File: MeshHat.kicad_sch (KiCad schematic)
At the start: 4 parts, among them J1 RPi_GPIO, U1 24LC256

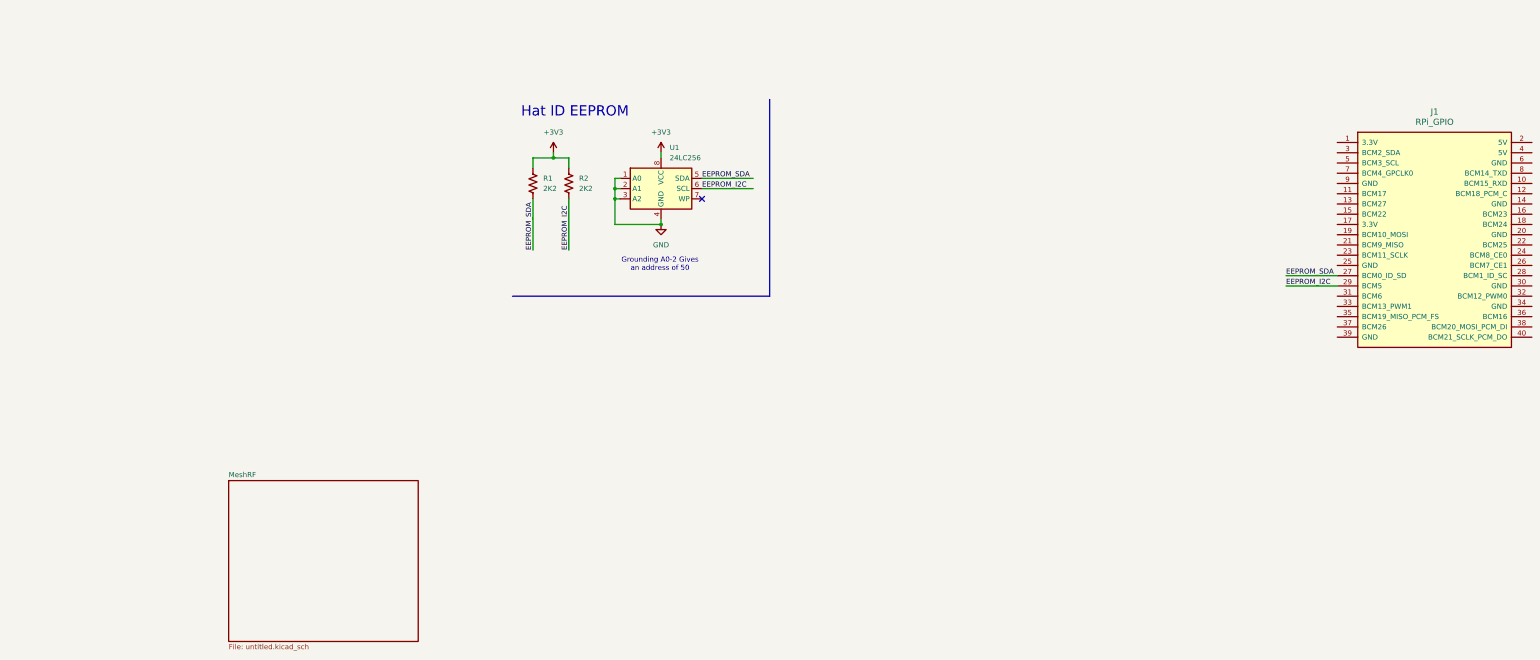
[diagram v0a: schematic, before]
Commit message: add the rest of the components and the OCD connections
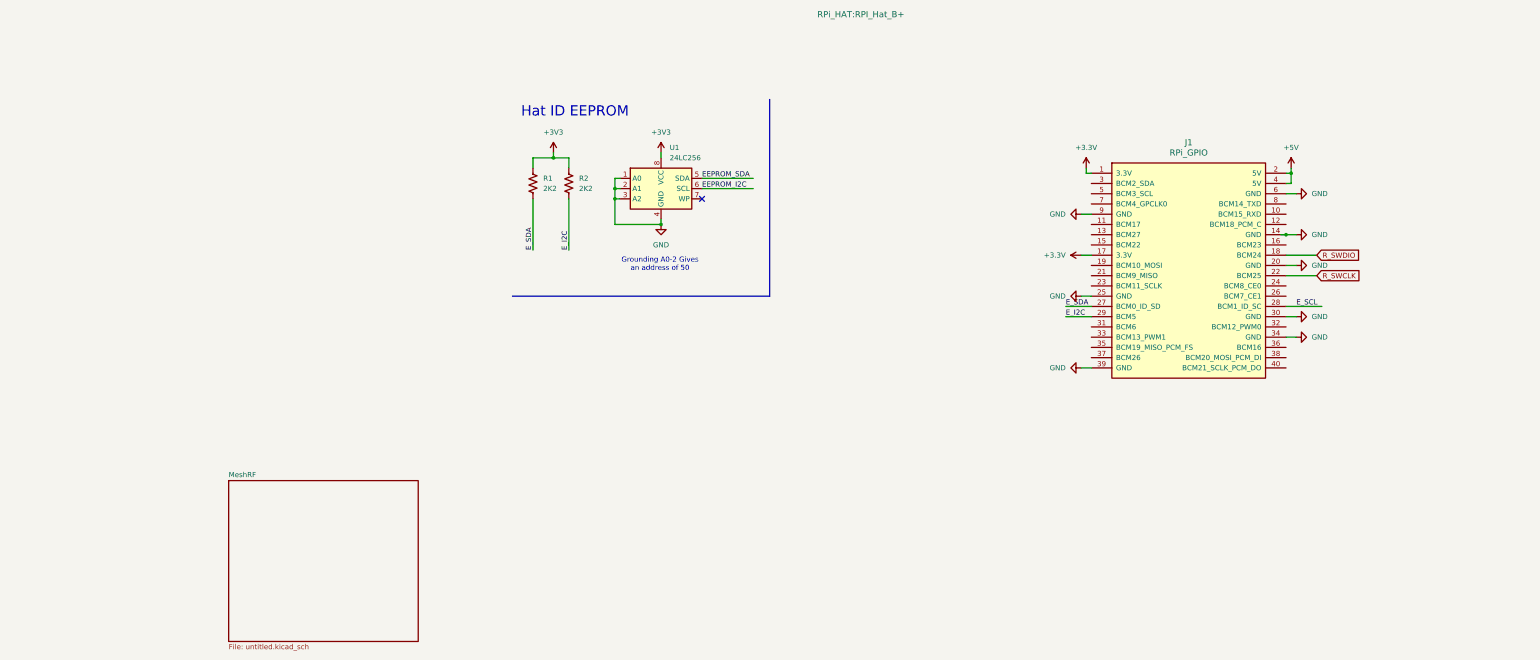
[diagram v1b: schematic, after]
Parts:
- J1: footprint (none) -> RPi_HAT:RPI_Hat_B+
- R1, R2: footprint Resistor_SMD:R_0201_0603Metric -> Resistor_SMD:R_0603_1608Metric
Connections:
- net EEPROM_I2C: no longer J1.29 (BCM5), R2.2
- net EEPROM_SDA: no longer J1.27 (BCM0_ID_SD), R1.2
- net GND: now also J1.14 (GND), J1.20 (GND), J1.25 (GND), J1.30 (GND), J1.34 (GND), J1.39 (GND), J1.6 (GND), J1.9 (GND)
- net +3.3V: now reaches J1.1 (3.3V)
- net +3.3V: now also J1.17 (3.3V)
- net R_SWDIO: now reaches J1.18 (BCM24)
- net +5V: now reaches J1.2 (5V)
- net +5V: now also J1.4 (5V)
- net R_SWCLK: now reaches J1.22 (BCM25)
- net E_SCL: now reaches J1.28 (BCM1_ID_SC)
- new net E_I2C: J1.29 (BCM5), R2.2
- new net E_SDA: J1.27 (BCM0_ID_SD), R1.2
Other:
- moved on the sheet: J1

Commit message: place all components
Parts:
- U1: footprint (none) -> Package_SO:SOIC-8_5.3x5.3mm_P1.27mm
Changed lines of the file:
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@@
 			)
 		)
-		(property "Footprint" ""
+		(property "Footprint" "Package_SO:SOIC-8_5.3x5.3mm_P1.27mm"
 			(at 49.53 34.29 0)
 			(effects

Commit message: more of the layout
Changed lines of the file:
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@@
 		(on_board yes)
 		(dnp no)
-		(fields_autoplaced yes)
 		(property "Reference" "J1"
 			(at 180.34 22.86 0)
@@
 		)
 		(property "Footprint" "RPi_HAT:RPI_Hat_B+"
-			(at 99.06 -8.89 0)
+			(at 168.402 18.034 0)
 			(effects
 				(font

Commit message: route more of the layout
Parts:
- added C15: 0U1, Capacitor_SMD:C_0603_1608Metric, symbol Device:C_Small
- J1: footprint RPi_HAT:RPI_Hat_B+ -> RPi Hat:RPI_Hat_B+
- U1: footprint Package_SO:SOIC-8_5.3x5.3mm_P1.27mm -> Package_SO:TSSOP-8_4.4x3mm_P0.65mm
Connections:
- net EEPROM_I2C is gone; now on net E_I2C: U1.6 (SCL)
- net EEPROM_SDA is gone; now on net E_SDA: U1.5 (SDA)
- net +3.3V: now also C15.1
- net GND: now also C15.2
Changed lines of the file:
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@@
+	(wire
+		(pts
+			(xy 68.58 49.53) (xy 68.58 50.8)
+		)
+		(stroke
+			(width 0)
+			(type default)
+		)
+	)
 	(wire
 		(pts
@@
 		(pts
 			(xy 156.21 30.48) (xy 154.94 30.48)
+		)
+		(stroke
+			(width 0)
+			(type default)
+		)
+	)
+	(wire
+		(pts
+			(xy 68.58 41.91) (xy 68.58 44.45)
 		)
 		(stroke
@@
 		)
 	)
-	(label "EEPROM_I2C"
+	(label "E_I2C"
 		(at 59.69 34.29 0)
 		(effects
@@
 		)
 	)
-	(label "EEPROM_SDA"
+	(label "E_SDA"
 		(at 59.69 31.75 0)
 		(effects
@@
 			)
 		)
-		(property "Footprint" "Package_SO:SOIC-8_5.3x5.3mm_P1.27mm"
+		(property "Footprint" "Package_SO:TSSOP-8_4.4x3mm_P0.65mm"
 			(at 49.53 34.29 0)
 			(effects
@@
 			)
 		)
-		(property "Footprint" "RPi_HAT:RPI_Hat_B+"
+		(property "Footprint" "RPi Hat:RPI_Hat_B+"
 			(at 168.402 18.034 0)
 			(effects
@@
 	)
 	(symbol
+		(lib_id "Device:C_Small")
+		(at 68.58 46.99 0)
+		(unit 1)
+		(exclude_from_sim no)
+		(in_bom yes)
+		(on_board yes)
+		(dnp no)
+		(fields_autoplaced yes)
+		(property "Reference" "C15"
+			(at 71.12 45.7262 0)
+			(effects
+				(font
+					(size 1.27 1.27)
+				)
+				(justify left)
+			)
+		)
+		(property "Value" "0U1"
+			(at 71.12 48.2662 0)
+			(effects
+				(font
+					(size 1.27 1.27)
+				)
+				(justify left)
+			)
+		)
+		(property "Footprint" "Capacitor_SMD:C_0603_1608Metric"
+			(at 68.58 46.99 0)
+			(effects
+				(font
+					(size 1.27 1.27)
+				)
+				(hide yes)
+			)
+		)
+		(property "Datasheet" "~"
+			(at 68.58 46.99 0)
+			(effects
+				(font
+					(size 1.27 1.27)
+				)
+				(hide yes)
+			)
+		)
+		(property "Description" "Unpolarized capacitor, small symbol"
+			(at 68.58 46.99 0)
+			(effects
+				(font
+					(size 1.27 1.27)
+				)
+				(hide yes)
+			)
+		)
+		(pin "1"
+		)
+		(pin "2"
+		)
+		(instances
+			(project "MeshHat"
+				(path "/ac5b0951-7b7b-41d2-b78c-2a2e4b31a9ff"
+					(reference "C15")
+					(unit 1)
+				)
+			)
+		)
+	)
+	(symbol
+		(lib_id "power:GND")
+		(at 68.58 50.8 0)
+		(unit 1)
+		(exclude_from_sim no)
+		(in_bom yes)
+		(on_board yes)
+		(dnp no)
+		(property "Reference" "#PWR033"
+			(at 68.58 57.15 0)
+			(effects
+				(font
+					(size 1.27 1.27)
+				)
+				(hide yes)
+			)
+		)
+		(property "Value" "GND"
+			(at 68.58 54.61 0)
+			(effects
+				(font
+					(size 1.27 1.27)
+				)
+			)
+		)
+		(property "Footprint" ""
+			(at 68.58 50.8 0)
+			(effects
+				(font
+					(size 1.27 1.27)
+				)
+				(hide yes)
+			)
+		)
+		(property "Datasheet" ""
+			(at 68.58 50.8 0)
+			(effects
+				(font
+					(size 1.27 1.27)
+				)
+				(hide yes)
+			)
+		)
+		(property "Description" "Power symbol creates a global label with name \"GND\" , ground"
+			(at 68.58 50.8 0)
+			(effects
+				(font
+					(size 1.27 1.27)
+				)
+				(hide yes)
+			)
+		)
+		(pin "1"
+		)
+		(instances
+			(project "MeshHat"
+				(path "/ac5b0951-7b7b-41d2-b78c-2a2e4b31a9ff"
+					(reference "#PWR033")
+					(unit 1)
+				)
+			)
+		)
+	)
+	(symbol
 		(lib_id "power:+5V")
 		(at 205.74 29.21 0)
@@
 					(unit 1)
 				)
+			)
+		)
+	)
+	(symbol
+		(lib_id "power:+1V1")
+		(at 68.58 41.91 0)
+		(unit 1)
+		(exclude_from_sim no)
+		(in_bom yes)
+		(on_board yes)
+		(dnp no)
+		(fields_autoplaced yes)
+		(property "Reference" "#PWR032"
+			(at 68.58 45.72 0)
+			(effects
+				(font
+					(size 1.27 1.27)
+				)
+				(hide yes)
+			)
+		)
+		(property "Value" "+3.3V"
+			(at 68.58 36.83 0)
+			(effects
+				(font
+					(size 1.27 1.27)
+				)
+			)
+		)
+		(property "Footprint" ""
+			(at 68.58 41.91 0)
+			(effects
+				(font
+					(size 1.27 1.27)
+				)
+				(hide yes)
+			)
+		)
+		(property "Datasheet" ""
+			(at 68.58 41.91 0)
+			(effects
+				(font
+					(size 1.27 1.27)
+				)
+				(hide yes)
+			)
+		)
+		(property "Description" "Power symbol creates a global label with name \"+1V1\""
+			(at 68.58 41.91 0)
+			(effects
+				(font
+					(size 1.27 1.27)
+				)
+				(hide yes)
+			)
+		)
+		(pin "1"
+		)
+		(instances
+			(project "MeshHat"
+				(path "/ac5b0951-7b7b-41d2-b78c-2a2e4b31a9ff"
+					(reference "#PWR032")
+					(unit 1)
+				)

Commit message: more cleanup of the schematic
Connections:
- net E_SCL: now also R2.2, U1.6 (SCL)
- net R_RX: now reaches J1.10 (BCM15_RXD)
- net R_TX: now reaches J1.8 (BCM14_TXD)
- removed net E_I2C: J1.29 (BCM5), R2.2, U1.6 (SCL)
- no-connect marks 1 -> 26
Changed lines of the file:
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@@
-	)
-	(junction
-		(at 204.47 45.72)
-		(diameter 0)
-		(color 0 0 0 0)
 	)
 	(junction
@@
 	)
 	(no_connect
+		(at 204.47 76.2)
+	)
+	(no_connect
+		(at 204.47 48.26)
+	)
+	(no_connect
+		(at 204.47 60.96)
+	)
+	(no_connect
+		(at 156.21 38.1)
+	)
+	(no_connect
+		(at 204.47 58.42)
+	)
+	(no_connect
+		(at 156.21 53.34)
+	)
+	(no_connect
 		(at 59.69 36.83)
 	)
+	(no_connect
+		(at 204.47 78.74)
+	)
+	(no_connect
+		(at 204.47 43.18)
+	)
+	(no_connect
+		(at 156.21 35.56)
+	)
+	(no_connect
+		(at 156.21 33.02)
+	)
+	(no_connect
+		(at 156.21 43.18)
+	)
+	(no_connect
+		(at 204.47 68.58)
+	)
+	(no_connect
+		(at 156.21 76.2)
+	)
+	(no_connect
+		(at 213.36 63.5)
+	)
+	(no_connect
+		(at 156.21 55.88)
+	)
+	(no_connect
+		(at 72.39 34.29)
+	)
+	(no_connect
+		(at 204.47 73.66)
+	)
+	(no_connect
+		(at 156.21 71.12)
+	)
+	(no_connect
+		(at 156.21 48.26)
+	)
+	(no_connect
+		(at 156.21 73.66)
+	)
+	(no_connect
+		(at 156.21 68.58)
+	)
+	(no_connect
+		(at 156.21 58.42)
+	)
+	(no_connect
+		(at 156.21 45.72)
+	)
+	(no_connect
+		(at 156.21 66.04)
+	)
+	(no_connect
+		(at 72.39 31.75)
+	)
 	(wire
 		(pts
@@
 	(wire
 		(pts
+			(xy 204.47 38.1) (xy 212.09 38.1)
+		)
+		(stroke
+			(width 0)
+			(type default)
+		)
+	)
+	(wire
+		(pts
 			(xy 154.94 30.48) (xy 154.94 29.21)
 		)
@@
 	(wire
 		(pts
+			(xy 204.47 45.72) (xy 207.01 45.72)
+		)
+		(stroke
+			(width 0)
+			(type default)
+		)
+	)
+	(wire
+		(pts
 			(xy 68.58 49.53) (xy 68.58 50.8)
 		)
@@
 	(wire
 		(pts
+			(xy 204.47 40.64) (xy 212.09 40.64)
+		)
+		(stroke
+			(width 0)
+			(type default)
+		)
+	)
+	(wire
+		(pts
 			(xy 17.78 36.83) (xy 17.78 49.53)
 		)
@@
 	(wire
 		(pts
-			(xy 204.47 45.72) (xy 203.2 45.72)
-		)
-		(stroke
-			(width 0)
-			(type default)
-		)
-	)
-	(wire
-		(pts
 			(xy 207.01 53.34) (xy 204.47 53.34)
 		)
@@
 	(wire
 		(pts
-			(xy 149.86 66.04) (xy 156.21 66.04)
-		)
-		(stroke
-			(width 0)
-			(type default)
-		)
-	)
-	(wire
-		(pts
 			(xy 153.67 40.64) (xy 156.21 40.64)
 		)
@@
 		(pts
 			(xy 204.47 35.56) (xy 207.01 35.56)
-		)
-		(stroke
-			(width 0)
-			(type default)
-		)
-	)
-	(wire
-		(pts
-			(xy 204.47 45.72) (xy 207.01 45.72)
 		)
 		(stroke
@@
 		)
 	)
-	(label "E_I2C"
+	(label "E_SCL"
 		(at 26.67 49.53 90)
 		(effects
@@
 		)
 	)
-	(label "E_I2C"
+	(label "E_SCL"
 		(at 59.69 34.29 0)
-		(effects
-			(font
-				(size 1.27 1.27)
-			)
-			(justify left bottom)
-		)
-	)
-	(label "E_I2C"
-		(at 149.86 66.04 0)
 		(effects
 			(font
@@
 			(hide yes)
 			(show_name no)
+			(do_not_autoplace no)
+			(effects
+				(font
+					(size 1.27 1.27)
+				)
+				(justify left)
+			)
+		)
+	)
+	(global_label "R_TX"
+		(shape input)
+		(at 212.09 38.1 0)
+		(fields_autoplaced yes)
+		(effects
+			(font
+				(size 1.27 1.27)
+			)
+			(justify left)
+		)
+		(property "Intersheetrefs" "${INTERSHEET_REFS}"
+			(at 219.4899 38.1 0)
+			(hide yes)
+			(show_name no)
+			(do_not_autoplace no)
+			(effects
+				(font
+					(size 1.27 1.27)
+				)
+				(justify left)
+			)
+		)
+	)
+	(global_label "R_RX"
+		(shape input)
+		(at 212.09 40.64 0)
+		(fields_autoplaced yes)
+		(effects
+			(font
+				(size 1.27 1.27)
+			)
+			(justify left)
+		)
+		(property "Intersheetrefs" "${INTERSHEET_REFS}"
+			(at 219.7923 40.64 0)
+			(hide yes)
+			(show_name no)

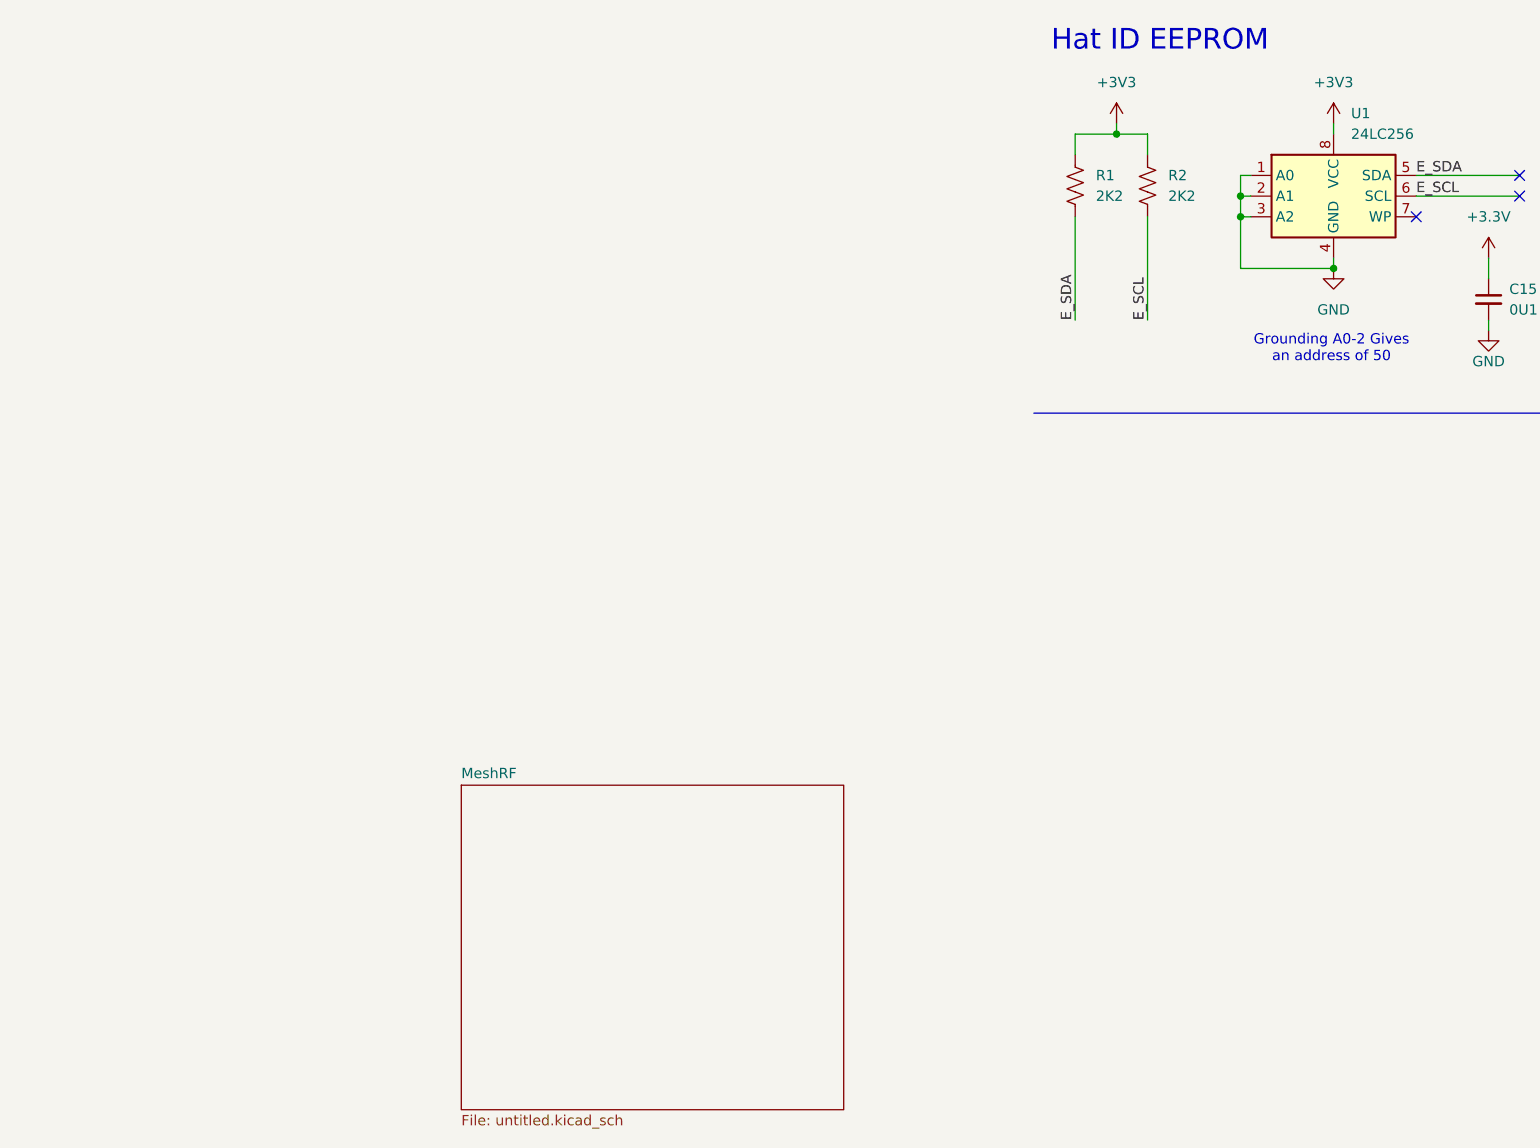
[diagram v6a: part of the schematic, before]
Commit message: add integration test arduino script
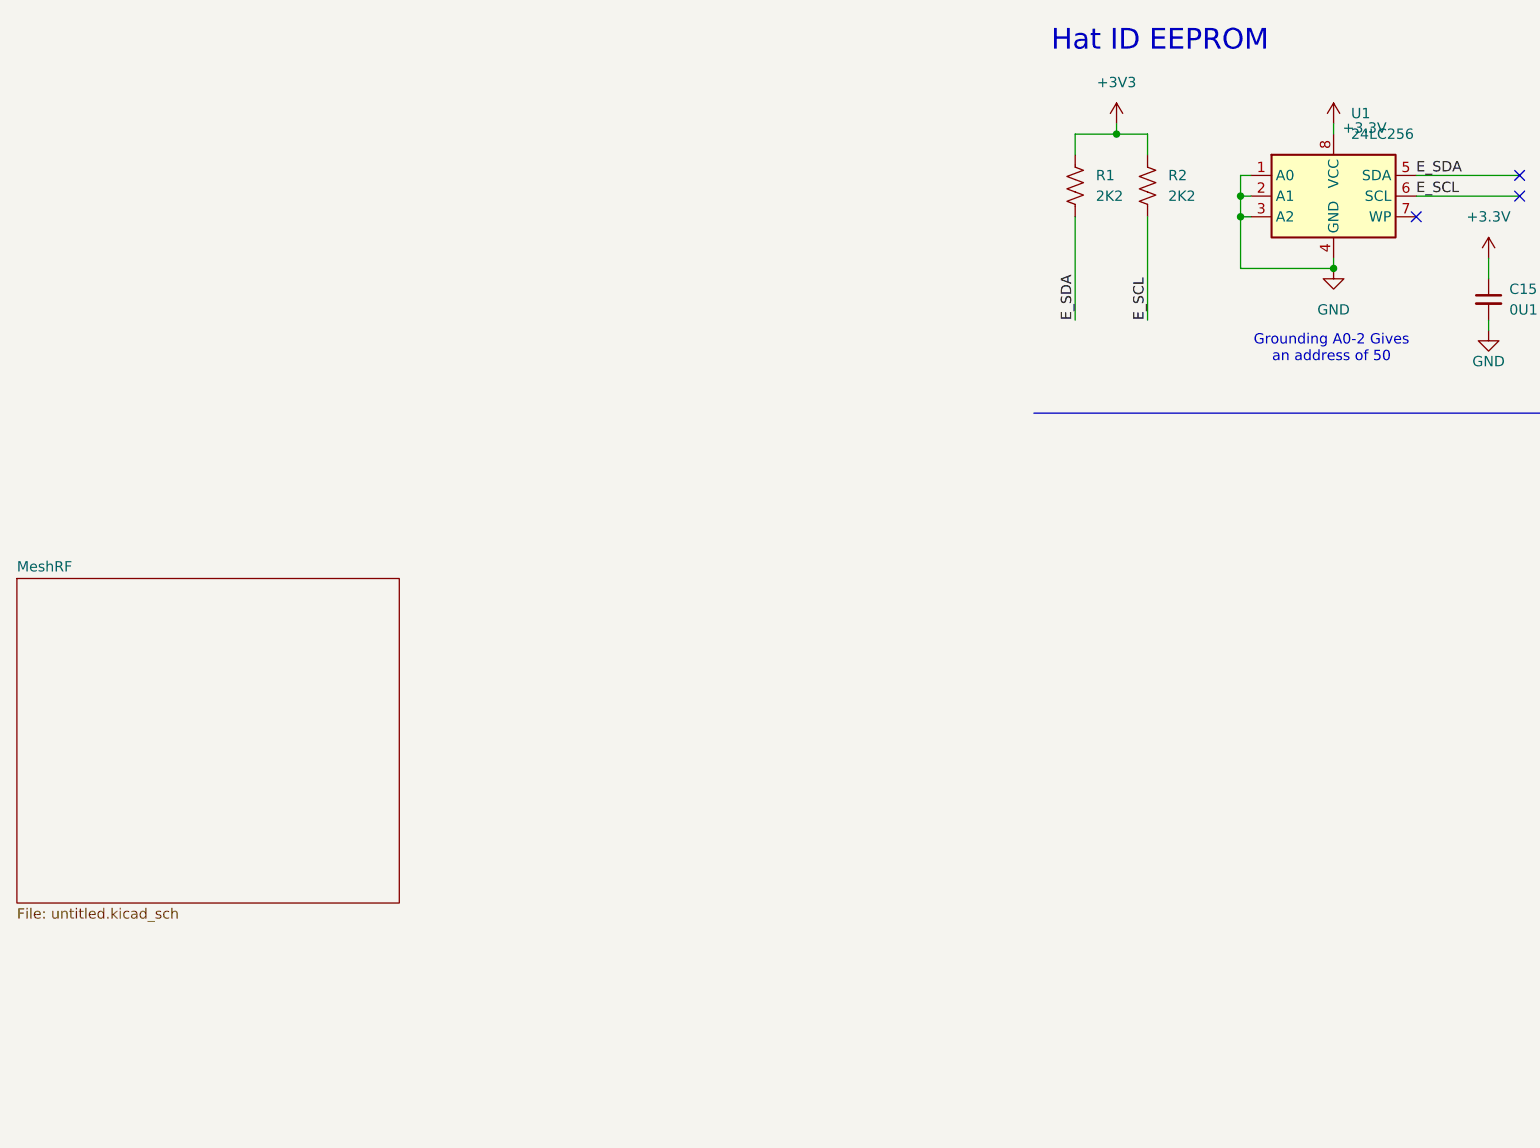
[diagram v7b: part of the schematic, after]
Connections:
- net +3.3V: now also U1.8 (VCC)
- net +3V3: no longer U1.8 (VCC)

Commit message: get most of the changes in
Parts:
- removed U1: 24LC256, Package_SO:TSSOP-8_4.4x3mm_P0.65mm, symbol Memory_EEPROM:24LC256
- added U3: CAT24C128, Package_SO:TSSOP-8_4.4x3mm_P0.65mm, symbol Memory_EEPROM:CAT24C128
- renumbered R2 to R1, R1 to R2
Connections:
- net +3V3 is gone; now on net +3.3V: R1.1, R2.1
- net +3.3V: now also U3.8 (VCC)
- net E_SCL: now also U3.6 (SCL)
- net E_SDA: now also U3.5 (SDA)
- net GND: now also U3.1 (A0), U3.2 (A1), U3.3 (A2), U3.4 (GND)
- net E_WP: now reaches J1.23 (BCM11_SCLK)
- net E_WP: now also U3.7 (WP)
- no-connect marks 26 -> 25
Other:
- note added: "Grounding A0-2 Gives an address of 0x50. This adheres to the "standard HAT+" spec https://github.com/raspberrypi/utils/tree/master/eeptools"
- note removed: "Grounding A0-2 Gives an address of 50"
